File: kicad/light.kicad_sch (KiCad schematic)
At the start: 216 parts, among them J1 USB_C, J2 SM03B-SRSS-TB, J3 Barrell Jack, J4 01x04, J5 Conn_01x09_MountingPin, J6 01x04, Q1 NMOS, Q2 NMOS, Q3 NMOS, SW1 Boot, SW2 Reset, SW3 On/Off, SW4 Mode, SW5 RotaryEncoder_Switch_MP, U1 RP2350A-QFN60, U2 TPS5405DR, U3 W25Q128JVS, U4 LBEE5KL1YN-814, U5 TPS2115ADRBR, U6 TPS2115ADRBR, U7 HDC1080, U8 MAX6818EAP_T, U9 PIR223D-S0, Y1 ABM8-272-T3

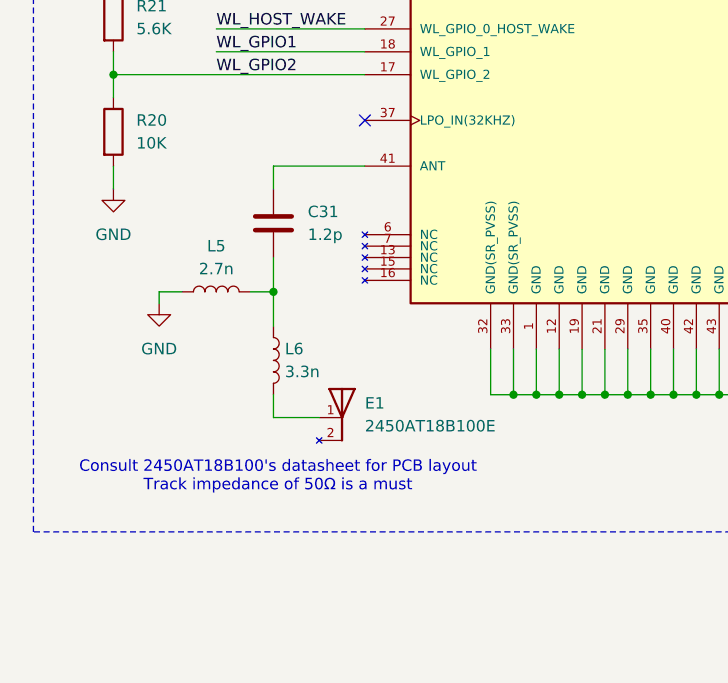
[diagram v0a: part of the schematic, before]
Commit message: add some more footprints
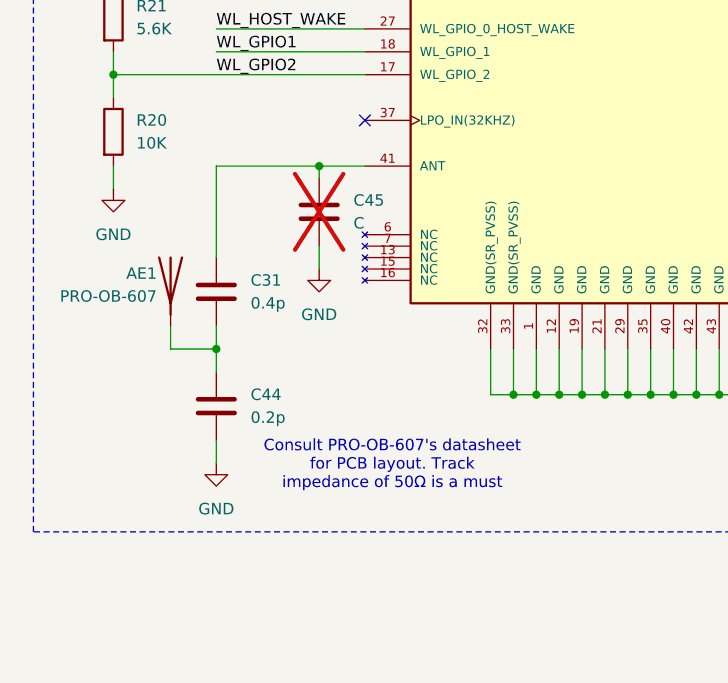
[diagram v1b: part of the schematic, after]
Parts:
- removed E1: 2450AT18B100E, 2450AT18B100E:XDCR_2450AT18B100E, symbol 2450AT18B100E:2450AT18B100E
- removed L5: 2.7n, symbol Device:L
- removed L6: 3.3n, symbol Device:L
- added AE1: PRO-OB-607, PRO-OB-607:PRO-OB-607, symbol Device:Antenna
- added C44: 0.2p, Capacitor_SMD:C_0402_1005Metric, symbol Device:C
- added C45: C, Capacitor_SMD:C_0402_1005Metric, symbol Device:C
- C31: value 1.2p -> 0.4p
- L1: footprint RF_Antenna:Abracon_PRO-OB-471 -> (none)
- L2: footprint (none) -> NRS5024:NRS5024T2R2NMGJ
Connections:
- net GND: now also C44.2, C45.2
- net at C31.2: now also AE1.1 (A), C44.1
- net at C31.1, U4.41 (ANT): now also C45.1
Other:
- note added: "Consult PRO-OB-607's datasheet for PCB layout. Track impedance of 50Ω is a must"
- note removed: "Consult 2450AT18B100's datasheet for PCB layout Track impedance of 50Ω is a must"

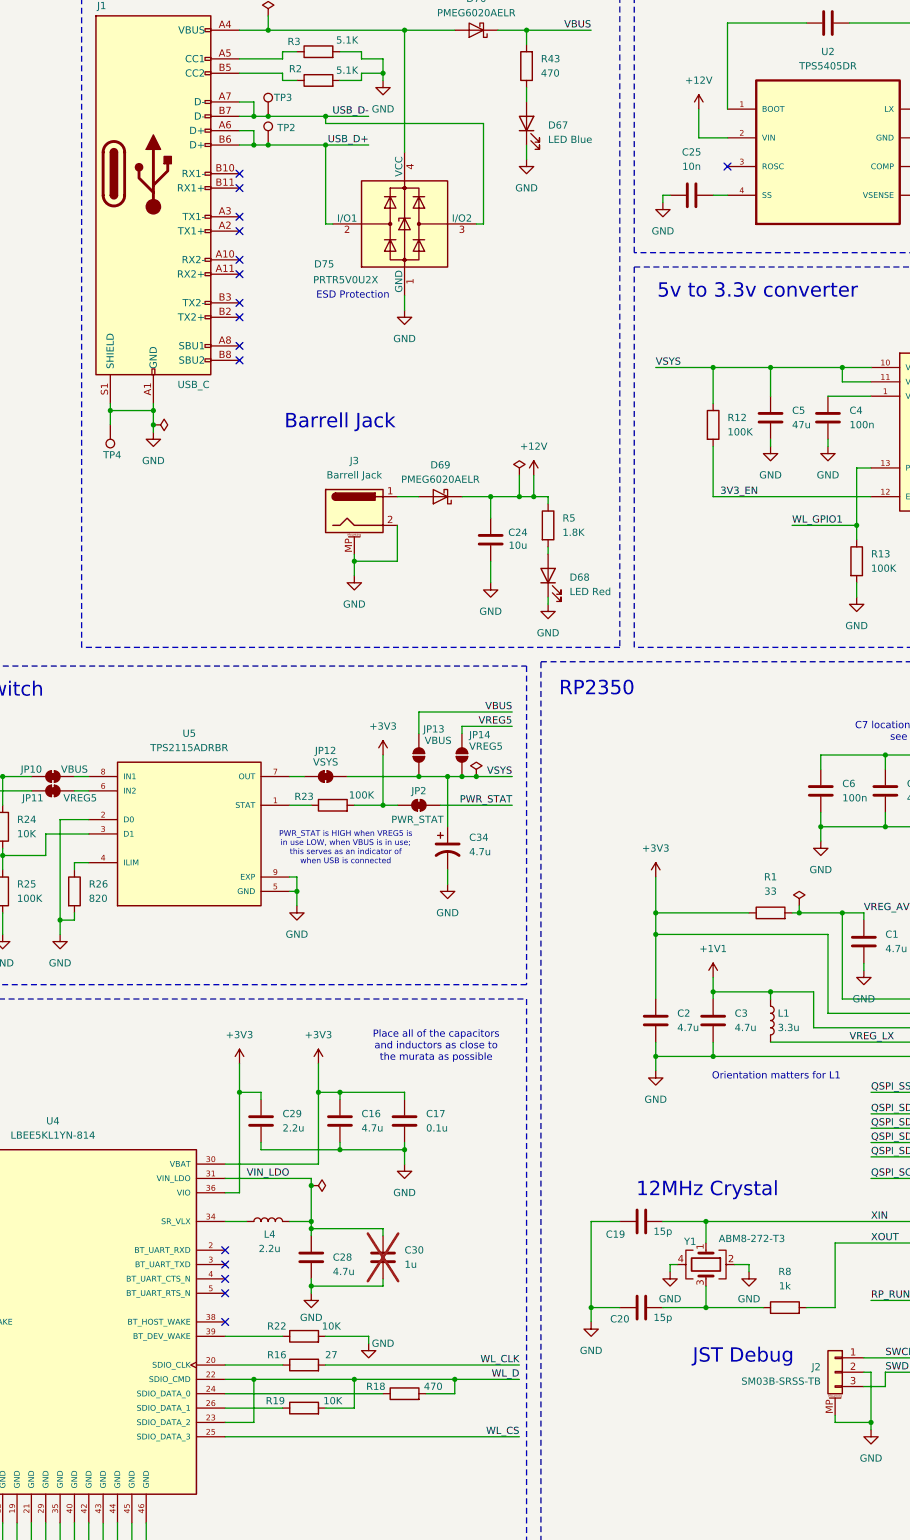
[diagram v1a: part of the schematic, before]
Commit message: create RP Inductor footprint; add AOTA-B201610S3R3-101-T 3D model
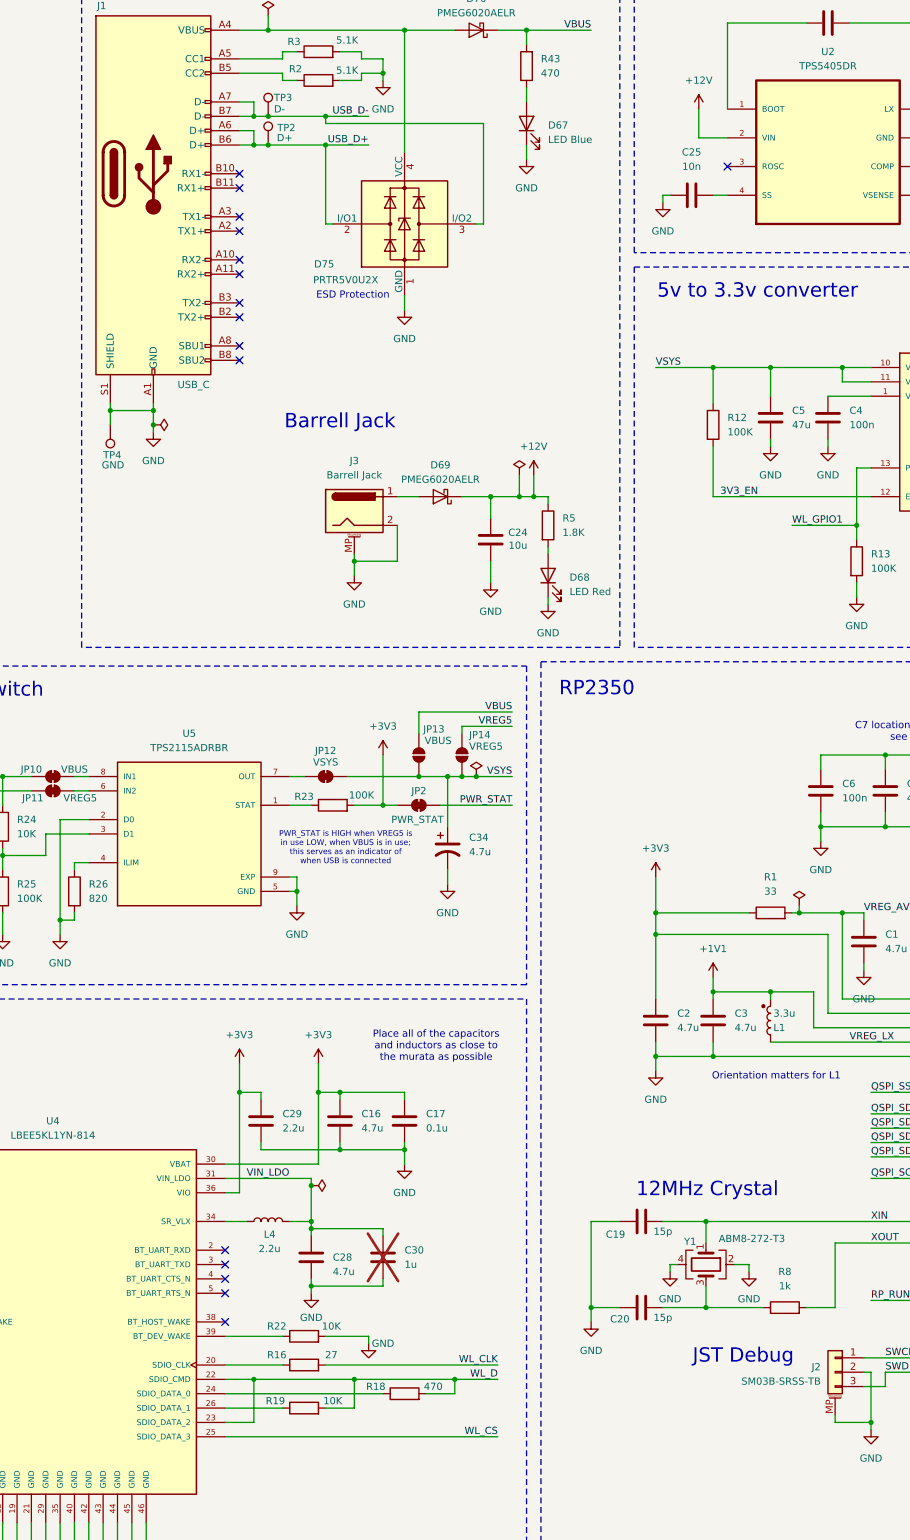
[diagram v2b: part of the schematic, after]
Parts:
- D1, D10, D11, D12, D13, D14, D15, D16, D17, D18, D19, D20, D21, D22, D23, D24, D25, D26, D27, D28, D29, D30, D31, D32, D33, D34, D35, D36, D37, D38, D39, D4, D40, D41, D42, D43, D44, D45, D46, D47, D48, D49, D5, D50, D51, D52, D53, D54, D55, D56, D57, D58, D59, D6, D60, D61, D62, D63, D64, D65, D66, D7, D8, D9: footprint WS2812B_1010:WS2812C-2020 -> WS2812B_1010:WS2812B_1010
- L1: footprint (none) -> AOTA-B201610S3R3-101-T:AOTA-B201610S3R3-101-T; symbol Device:L -> Device:L_Polarized
- TP1, TP5, TP6, TP7, TP8, TP9: footprint TestPoint:TestPoint_Pad_D2.0mm -> TestPoint:TestPoint_Pad_D1.0mm
- TP10: footprint TestPoint:TestPoint_Pad_2.0x2.0mm -> TestPoint:TestPoint_Pad_1.0x1.0mm
- TP2: value TestPoint -> D+; footprint TestPoint:TestPoint_Pad_D2.0mm -> TestPoint:TestPoint_Pad_D1.0mm
- TP3: value TestPoint -> D-; footprint TestPoint:TestPoint_Pad_D2.0mm -> TestPoint:TestPoint_Pad_D1.0mm
- TP4: value TestPoint -> GND; footprint TestPoint:TestPoint_Pad_D2.0mm -> TestPoint:TestPoint_Pad_D1.0mm
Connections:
- net +1V1: now also L1.2; no longer L1.1
- net VREG_LX: now also L1.1; no longer L1.2

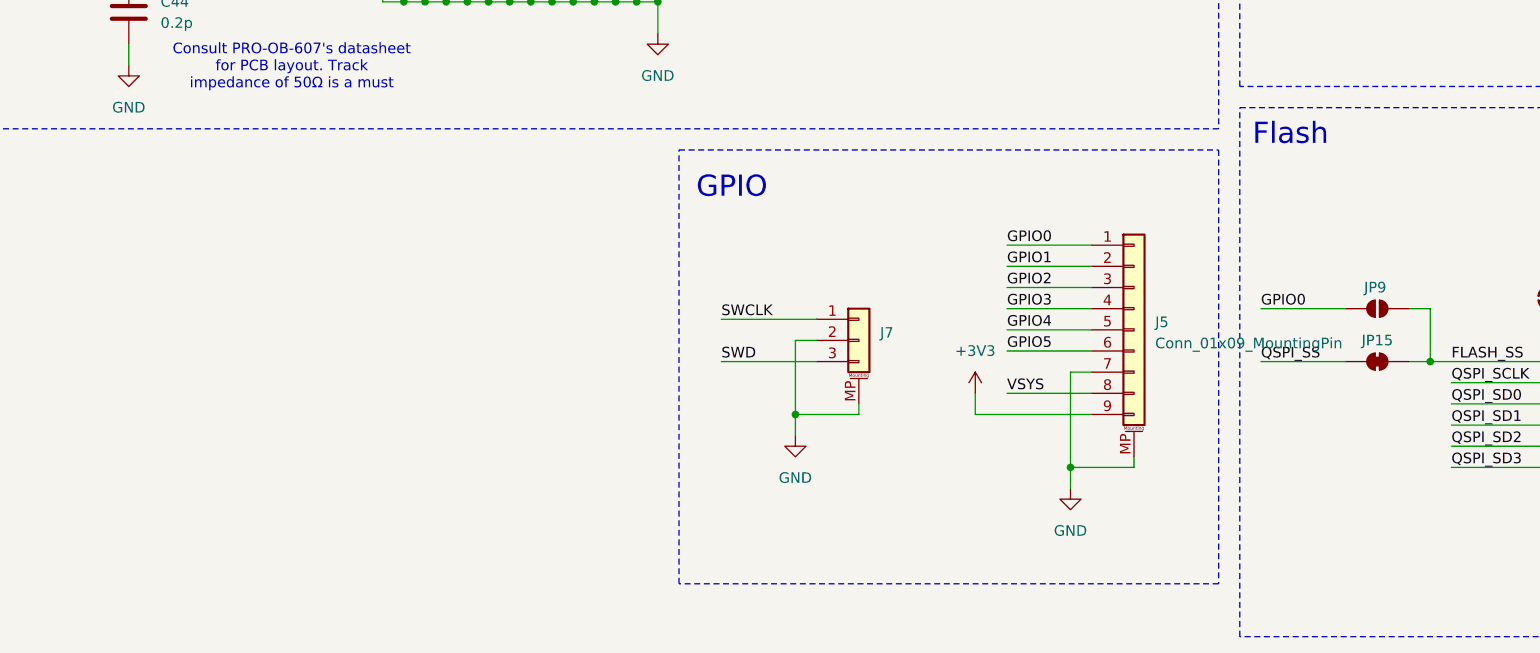
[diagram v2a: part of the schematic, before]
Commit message: set inductors
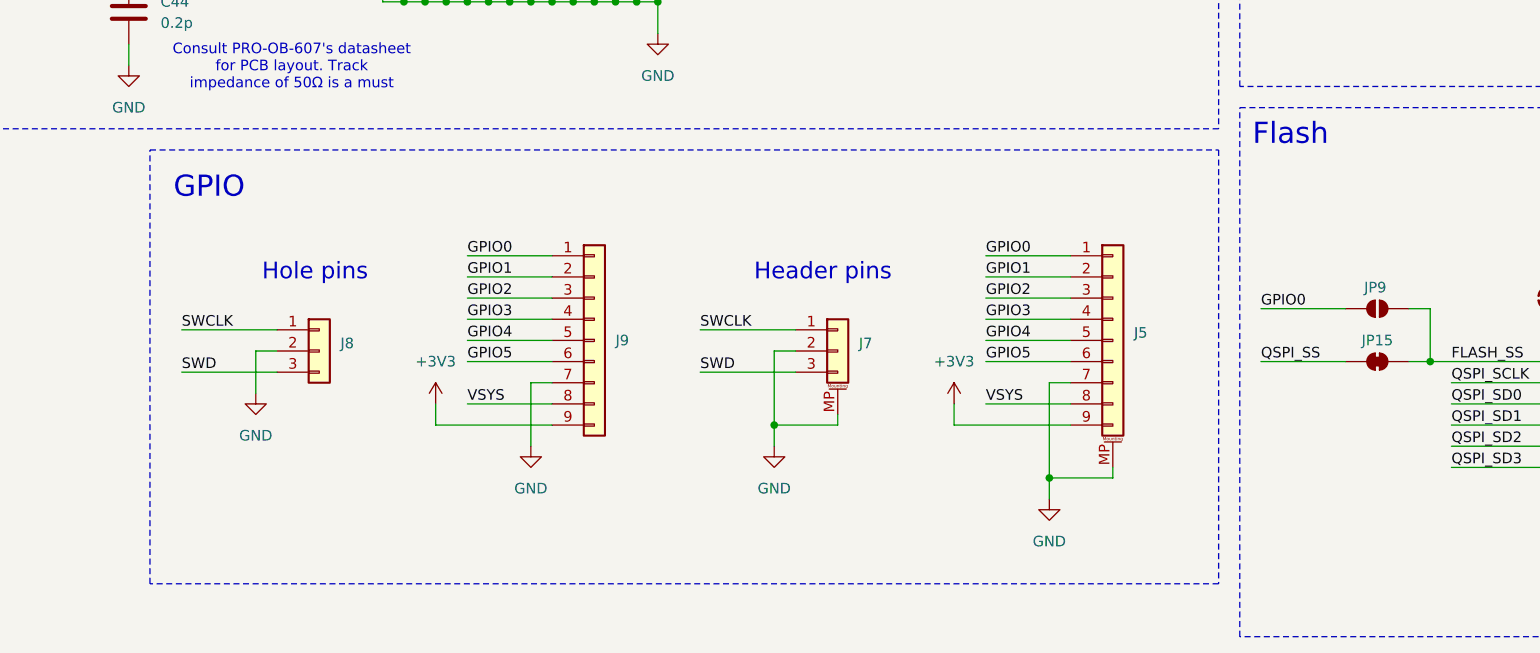
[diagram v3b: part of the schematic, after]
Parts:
- added J8: ~, Connector_PinSocket_2.54mm:PinSocket_1x03_P2.54mm_Vertical, symbol Connector_Generic:Conn_01x03
- added J9: Conn_01x09_MountingPin, Connector_PinSocket_2.54mm:PinSocket_1x09_P2.54mm_Vertical, symbol Connector_Generic:Conn_01x09
- L3: footprint (none) -> LQH5BPZ4R7NT0L:LQH5BPZ4R7NT0L_5x5mm
- L4: footprint (none) -> Inductor_SMD:L_0603_1608Metric; MFR.Part # (none) -> LQM18PN2R2MGH
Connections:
- net +3V3: now also J9.9 (Pin_9)
- net GND: now also J8.2 (Pin_2), J9.7 (Pin_7)
- net GPIO0: now also J9.1 (Pin_1)
- net GPIO1: now also J9.2 (Pin_2)
- net GPIO2: now also J9.3 (Pin_3)
- net GPIO3: now also J9.4 (Pin_4)
- net GPIO4: now also J9.5 (Pin_5)
- net GPIO5: now also J9.6 (Pin_6)
- net SWCLK: now also J8.1 (Pin_1)
- net SWD: now also J8.3 (Pin_3)
- net VSYS: now also J9.8 (Pin_8)
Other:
- note added: "Header pins"
- note added: "Hole pins"
- moved on the sheet: J5, J7

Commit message: finish footprint selection
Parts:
- removed J7: ~, Connector_JST:JST_SH_SM03B-SRSS-TB_1x03-1MP_P1.00mm_Horizontal, symbol Connector_Generic_MountingPin:Conn_01x03_MountingPin
- C34, C38: footprint Capacitor_SMD:CP_Elec_4x5.4 -> Capacitor_SMD:C_0603_1608Metric; symbol Device:C_Polarized_US -> Device:C
- Q1, Q2, Q3: footprint (none) -> Package_TO_SOT_SMD:SOT-23
- R1: footprint (none) -> Resistor_SMD:R_0603_1608Metric
- R10, R13, R14, R15, R2, R3, R36, R37, R4, R6, R8, R9: footprint (none) -> Resistor_SMD:R_0201_0603Metric
- R11, R16, R17, R18, R19, R20, R21, R22, R23, R24, R25, R26, R40, R41, R43, R44, R5, R7: footprint (none) -> Resistor_SMD:R_0402_1005Metric
- R12: footprint (none) -> Resistor_SMD:R_0402_1005Metric_Pad0.72x0.64mm_HandSolder
- R27, R28, R29, R30, R31, R32, R33, R34, R35: footprint (none) -> Capacitor_SMD:C_0402_1005Metric
- R38, R39, R42: footprint (none) -> Resistor_SMD:R_0402_1005Metric; now left out of the parts list
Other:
- moved on the sheet: C10, C11, C12, C13, C14, C15, C9, D73, J8, J9, R33, R34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

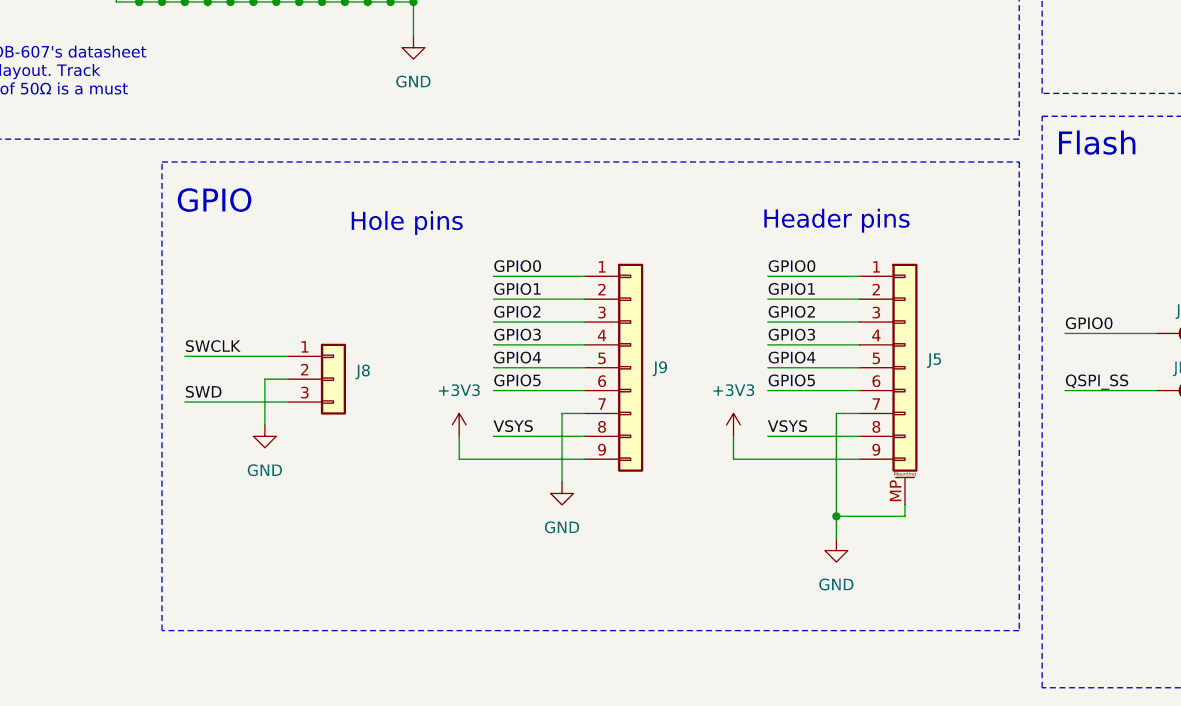
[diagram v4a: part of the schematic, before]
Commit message: fix wrong pin name on footprints
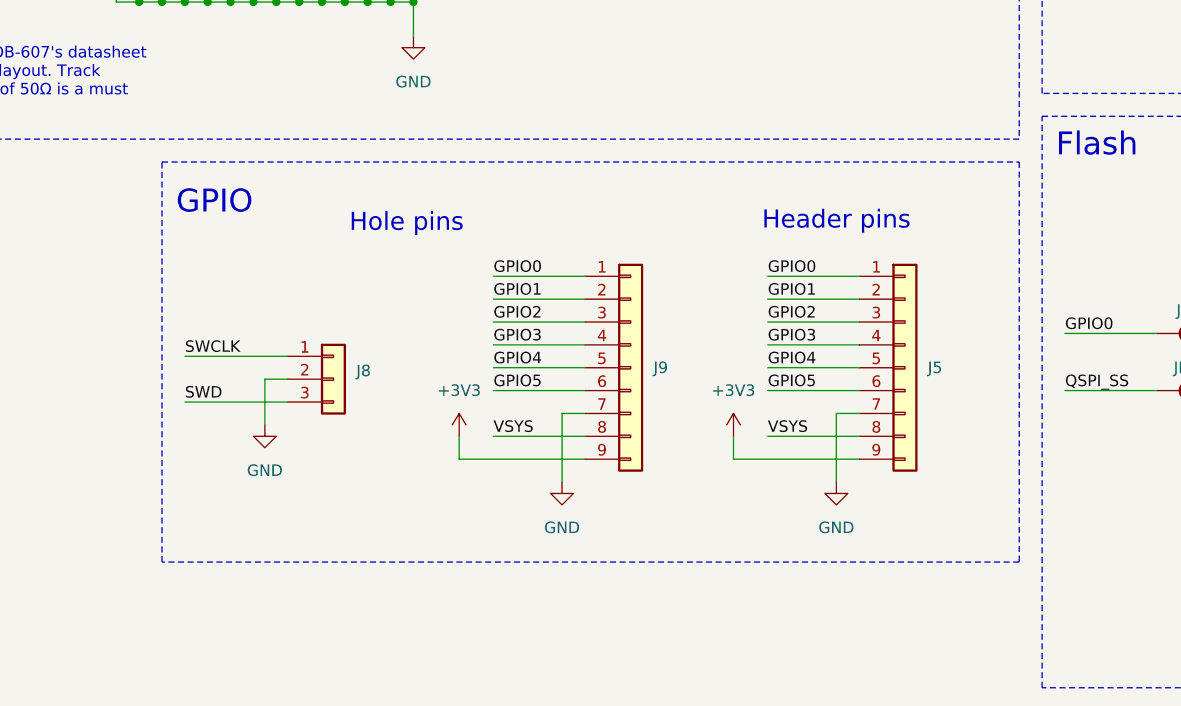
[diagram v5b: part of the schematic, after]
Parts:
- J5: footprint Connector_PinSocket_2.54mm:PinSocket_1x08_P2.54mm_Horizontal -> Connector_PinSocket_2.54mm:PinSocket_1x09_P2.54mm_Horizontal; symbol Connector_Generic_MountingPin:Conn_01x09_MountingPin -> Connector_Generic:Conn_01x09
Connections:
- net GND: no longer J5.MP (MountPin)
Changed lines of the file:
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@@
 	(rectangle
 		(start 129.54 439.42)
-		(end 224.79 491.49)
+		(end 224.79 483.87)
 		(stroke
 			(width 0)
@@
 	)
 	(junction
-		(at 204.47 478.79)
-		(diameter 0)
-		(color 0 0 0 0)
-	)
-	(junction
 		(at 283.21 454.66)
 		(diameter 0)
@@
 	(wire
 		(pts
-			(xy 204.47 478.79) (xy 204.47 481.33)
+			(xy 204.47 467.36) (xy 204.47 474.98)
 		)
 		(stroke
@@
 	(wire
 		(pts
-			(xy 212.09 477.52) (xy 212.09 478.79)
-		)
-		(stroke
-			(width 0)
-			(type default)
-		)
-	)
-	(wire
-		(pts
 			(xy 323.85 293.37) (xy 335.28 293.37)
 		)
@@
 	(wire
 		(pts
-			(xy 212.09 478.79) (xy 204.47 478.79)
-		)
-		(stroke
-			(width 0)
-			(type default)
-		)
-	)
-	(wire
-		(pts
 			(xy 469.9 161.29) (xy 469.9 163.83)
 		)
@@
 	(wire
 		(pts
-			(xy 204.47 467.36) (xy 204.47 478.79)
-		)
-		(stroke
-			(width 0)
-			(type default)
-		)
-	)
-	(wire
-		(pts
 			(xy 485.14 345.44) (xy 485.14 347.98)
 		)
@@
 	)
 	(symbol
-		(lib_id "Connector_Generic_MountingPin:Conn_01x09_MountingPin")
+		(lib_id "Connector_Generic:Conn_01x09")
 		(at 212.09 462.28 0)
 		(unit 1)
@@
 		(fields_autoplaced yes)
 		(property "Reference" "J5"
-			(at 214.63 461.3655 0)
+			(at 214.63 462.2799 0)
 			(effects
 				(font
@@
 			)
 		)
-		(property "Footprint" "Connector_PinSocket_2.54mm:PinSocket_1x08_P2.54mm_Horizontal"
+		(property "Footprint" "Connector_PinSocket_2.54mm:PinSocket_1x09_P2.54mm_Horizontal"
 			(at 212.09 462.28 0)
 			(effects
@@
 			)
 		)
-		(property "Description" "Generic connectable mounting pin connector, single row, 01x09, script generated (kicad-library-utils/schlib/autogen/connector/)"
+		(property "Description" "Generic connector, single row, 01x09, script generated (kicad-library-utils/schlib/autogen/connector/)"
 			(at 212.09 462.28 0)
 			(effects
@@
 		(pin "5"
 		)
-		(pin "MP"
-		)
 		(pin "8"
 		)
@@
 		(exclude_from_sim no)
 		(in_bom no)
-		(on_board no)
+		(on_board yes)
 		(dnp yes)
 		(fields_autoplaced yes)
@@
 		(exclude_from_sim no)
 		(in_bom no)
-		(on_board no)
+		(on_board yes)
 		(dnp yes)
 		(fields_autoplaced yes)
@@
 		(exclude_from_sim no)
 		(in_bom no)
-		(on_board no)
+		(on_board yes)
 		(dnp yes)
-		(fields_autoplaced yes)
 		(property "Reference" "R39"
 			(at 453.39 218.4399 0)
@@
 	(symbol
 		(lib_id "power:GND")
-		(at 204.47 481.33 0)
+		(at 204.47 474.98 0)
 		(unit 1)
 		(exclude_from_sim no)
@@
 		(fields_autoplaced yes)
 		(property "Reference" "#PWR075"
-			(at 204.47 487.68 0)
+			(at 204.47 481.33 0)
 			(effects
 				(font
@@
 		)
 		(property "Value" "GND"
-			(at 204.47 486.41 0)
+			(at 204.47 480.06 0)
 			(effects
 				(font
@@
 		)
 		(property "Footprint" ""
-			(at 204.47 481.33 0)
+			(at 204.47 474.98 0)
 			(effects
 				(font
@@
 		)
 		(property "Datasheet" ""
-			(at 204.47 481.33 0)
+			(at 204.47 474.98 0)
 			(effects
 				(font
@@
 		)
 		(property "Description" "Power symbol creates a global label with name \"GND\" , ground"
-			(at 204.47 481.33 0)
+			(at 204.47 474.98 0)
 			(effects
 				(font
